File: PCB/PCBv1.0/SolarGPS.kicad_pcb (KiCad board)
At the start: 2 copper layers, 64 x 27 mm, 64 parts, among them J1 Conn_01x10_Female, J2 Solar1+, J3 GND, J4 Conn_02x05_Odd_Even, J5 Solar2+, J6 GND, J7 Screw_Terminal_01x01, U1 BQ25505, U2 MAX-M8Q, U3 MAX40200AUK, U4 STM32WB5MMGH6TR, U5 BQ25505, U6 LIS3DH, U7 TPS63802

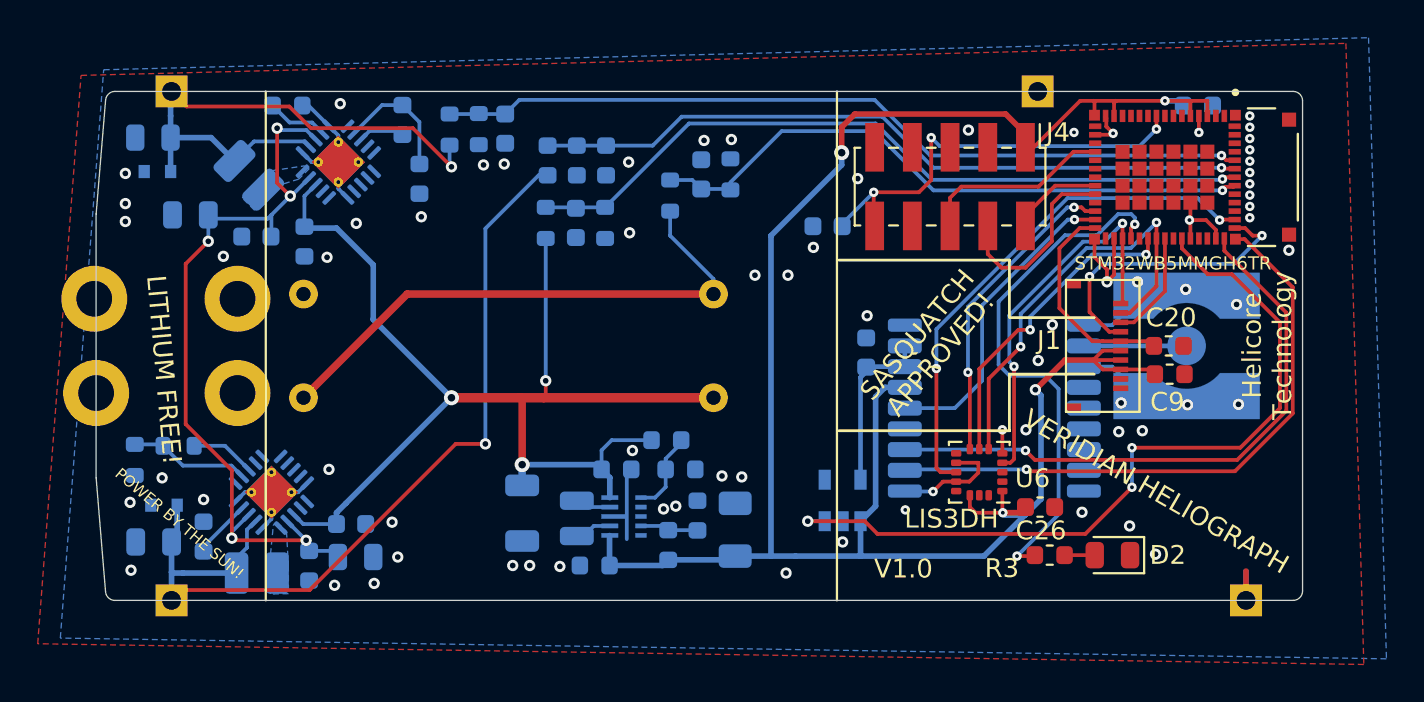
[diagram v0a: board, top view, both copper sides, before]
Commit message: Update PCB1.0 with new layout
Reverse the LCD direction for more space on the GPS signal
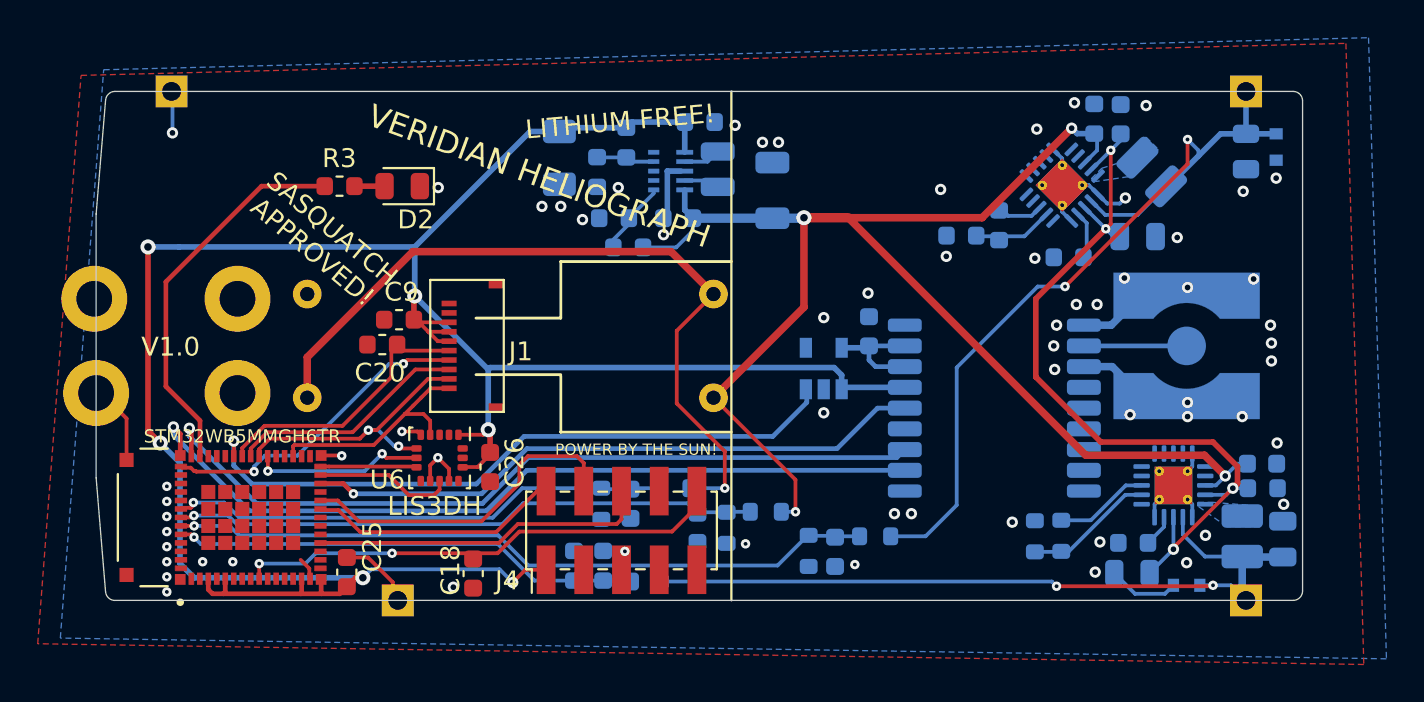
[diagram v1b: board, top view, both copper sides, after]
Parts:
- C18, C25: moved to F.Cu
- R3: value 1k -> 400
- R4: value 470k -> 412k
- U2: value MAX-M8Q -> MAX-M10Q
- moved C1 59.9 mm to (112.0, 73.8), turned to 90 degrees
- moved D3 59.4 mm to (111.6, 53.0), turned to 270 degrees
- moved C3 58.0 mm to (110.0, 53.2), turned to 270 degrees
- moved J2 57.0 mm to (110.0, 50.0)
- moved J5 57.0 mm to (110.0, 77.0)
- moved U4 54.7 mm to (55.6, 72.6), turned to 90 degrees
- moved D4 54.4 mm to (106.8, 76.2)
- moved L1 52.3 mm to (109.8, 73.6), turned to 90 degrees
- moved C25 51.5 mm to (62.3, 75.5), turned to 90 degrees
- moved C19 50.8 mm to (110.9, 71.0), turned to 180 degrees
- moved C2 50.3 mm to (104.2, 57.7), turned to 180 degrees
- moved C13 49.3 mm to (104.0, 74.0), turned to 180 degrees
- moved C11 48.4 mm to (110.8, 69.8)
- moved ROV1 47.9 mm to (98.8, 73.6), turned to 90 degrees
- moved L3 47.9 mm to (105.0, 54.3), turned to 135 degrees
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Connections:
- U4 pad 28: LIS_CS -> GPS_EXINT
- U4 pad 29: GPS_EXINT -> LIS_INT
- U4 pad 30: DISP_EN -> LIS_CS
- U4 pad 33: GND -> Net-(U4-Pad33)
- U4 pad 35: LED -> Net-(U4-Pad35)
- U4 pad 40: Net-(U4-Pad40) -> DISP_EN
- U4 pad 42: GND -> Net-(U4-Pad42)
- U4 pad 45: GND -> LED
- U4 pad 49: LIS_INT -> Net-(U4-Pad49)
- U4 pad 55: SOLAR_SENSE2 -> SOLAR_SENSE1
- U4 pad 56: SOLAR_SENSE1 -> SOLAR_SENSE2
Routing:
- net LIS_INT: track 27.7 -> 7.34 mm, vias 2 -> 0
- net VDD: track 109.2 -> 128.2 mm, vias 4 -> 6
- net GPS_EXINT: track 16.6 -> 33.1 mm
- net SOLAR1+: track 29.7 -> 44.4 mm, vias 1 -> 2
- net VBAT: track 64.7 -> 79.3 mm, vias 3 -> 4
- net SOLAR_SENSE2: track 38.2 -> 25.1 mm
- net VBATMID: track 29.6 -> 41.3 mm, vias 0 -> 1
- net LIS_CS: track 16.6 -> 5.11 mm, vias 2 -> 0
- net GPS_UART_MISO: track 32.7 -> 43.4 mm
- net GPS_UART_MOSI: track 32.1 -> 42.6 mm
- net VBAT_SENSE: track 39.7 -> 31.1 mm
- net /SWDIO: track 4.91 -> 13.4 mm
- net SPI_CLK: track 20.7 -> 12.3 mm, vias 2 -> 0
- net SPI_MOSI: track 23.0 -> 14.9 mm
- net /SWDCLK: track 10.3 -> 18.1 mm
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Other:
- board text removed: "Helicore Technology"

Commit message: Cost reduction, remove second mppt
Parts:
- removed C1, C21: 4.7uF, Capacitor_SMD:C_0805_2012Metric
- removed C10, C11, C13, C22: 10nF, Capacitor_SMD:C_0603_1608Metric
- removed L1: 22uH, Inductor_SMD:L_1008_2520Metric
- removed R7, R8: 1M, Resistor_SMD:R_0603_1608Metric
- removed ROV1: 4.32M, Resistor_SMD:R_0603_1608Metric
- removed ROV2: 8.66M, Resistor_SMD:R_0603_1608Metric
- removed U1: BQ25505, Package_DFN_QFN:QFN-20-1EP_3.5x3.5mm_P0.5mm_EP2x2mm_ThermalVias
- added D1: Schottky, Diode_SMD:D_SOD-323_HandSoldering, B.Cu at (110.0, 73.6)
- D3: value 5.1V -> Schottky; footprint Diode_SMD:D_SOD-523 -> Diode_SMD:D_SOD-323_HandSoldering
- moved C19 21.0 mm to (103.4, 51.4), turned to 270 degrees
- moved D4 20.6 mm to (111.8, 56.2), turned to 270 degrees
- moved C3 3.21 mm to (110.0, 56.4)
- moved D3 1.60 mm to (110.0, 52.9), turned to 90 degrees
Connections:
- C3 pad 1: SOLAR1+ -> SOLAR+
- D3 pad 1: SOLAR1+ -> SOLAR+
- D3 pad 2: GND -> Net-(D3-Pad2)
- D4 pad 1: SOLAR2+ -> SOLAR+
- J2 pad 1: SOLAR1+ -> Net-(D3-Pad2)
- J5 pad 1: SOLAR2+ -> Net-(D1-Pad2)
- L3 pad 1: SOLAR1+ -> SOLAR+
- R14 pad 2: SOLAR1+ -> SOLAR+
- U5 pad 2: SOLAR1+ -> SOLAR+
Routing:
- net SOLAR+: track 0.00 -> 58.2 mm, vias 0 -> 2
- net SOLAR1+: track 44.4 -> 0.00 mm, vias 2 -> 0
- net SOLAR2+: track 40.5 -> 0.00 mm, vias 2 -> 0
- net VSTOR: track 43.1 -> 9.30 mm, vias 4 -> 2
- net VBAT: track 79.3 -> 49.9 mm, vias 4 -> 3
- net SOLAR_SENSE2: track 25.1 -> 0.00 mm, vias 1 -> 0
- net VDD: track 128.2 -> 110.7 mm, vias 6 -> 7
- net GND: track 46.8 -> 37.8 mm, vias 64 -> 89
- net Net-(ROV1-Pad1): track 6.92 -> 0.00 mm
- net Net-(ROV2-Pad1): track 5.03 -> 0.00 mm
- net VBATMID: track 41.3 -> 43.7 mm
- net Net-(D1-Pad2): track 0.00 -> 1.88 mm
- net Net-(C13-Pad1): track 1.71 -> 0.00 mm
- net Net-(D3-Pad2): track 0.00 -> 1.43 mm
- removed copper zone on B.Cu, net Net-(L1-Pad2)

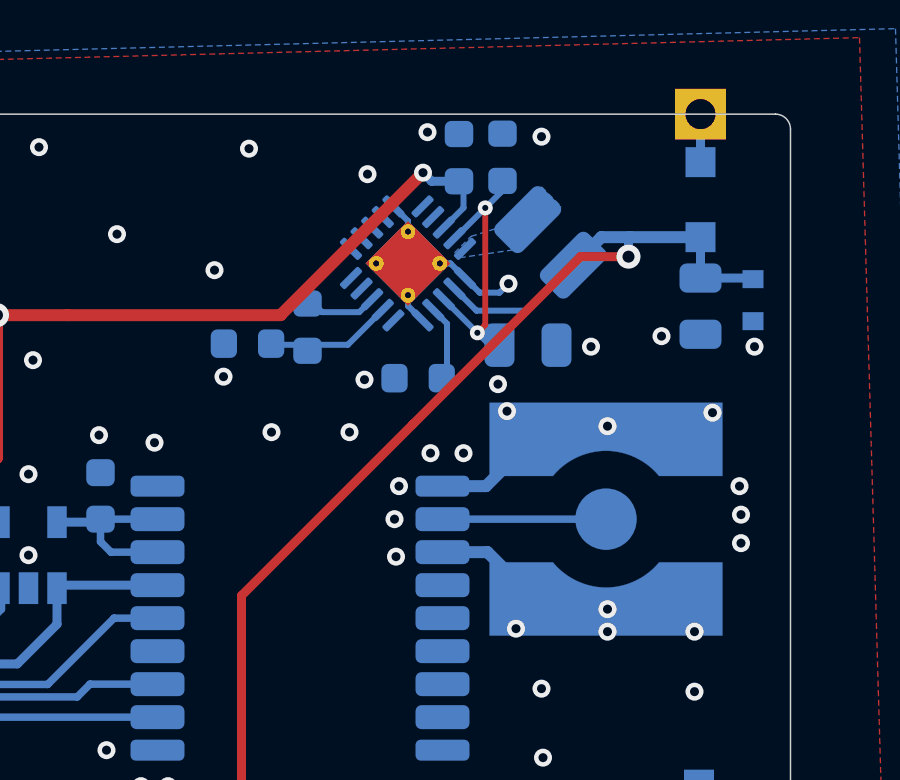
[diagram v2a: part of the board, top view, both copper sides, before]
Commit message: Update BOM, start treebuilders
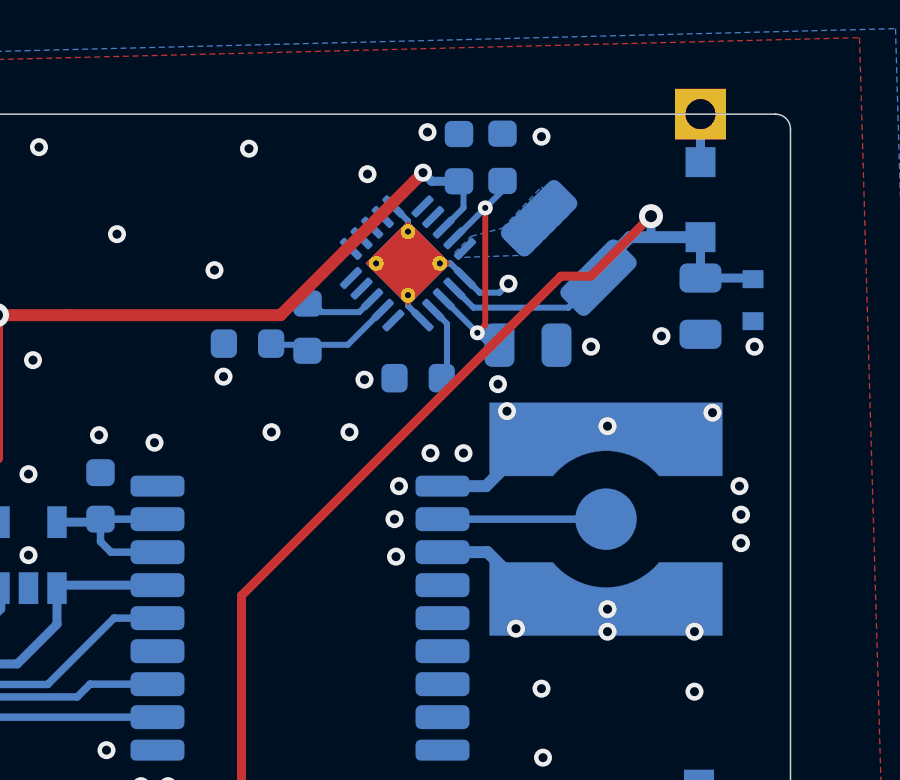
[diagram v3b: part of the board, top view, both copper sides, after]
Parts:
- L3: footprint Inductor_SMD:L_1008_2520Metric -> Inductor_SMD:L_1210_3225Metric
- moved L3 0.64 mm to (105.6, 54.5)
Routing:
- net SOLAR+: track 58.2 -> 59.1 mm

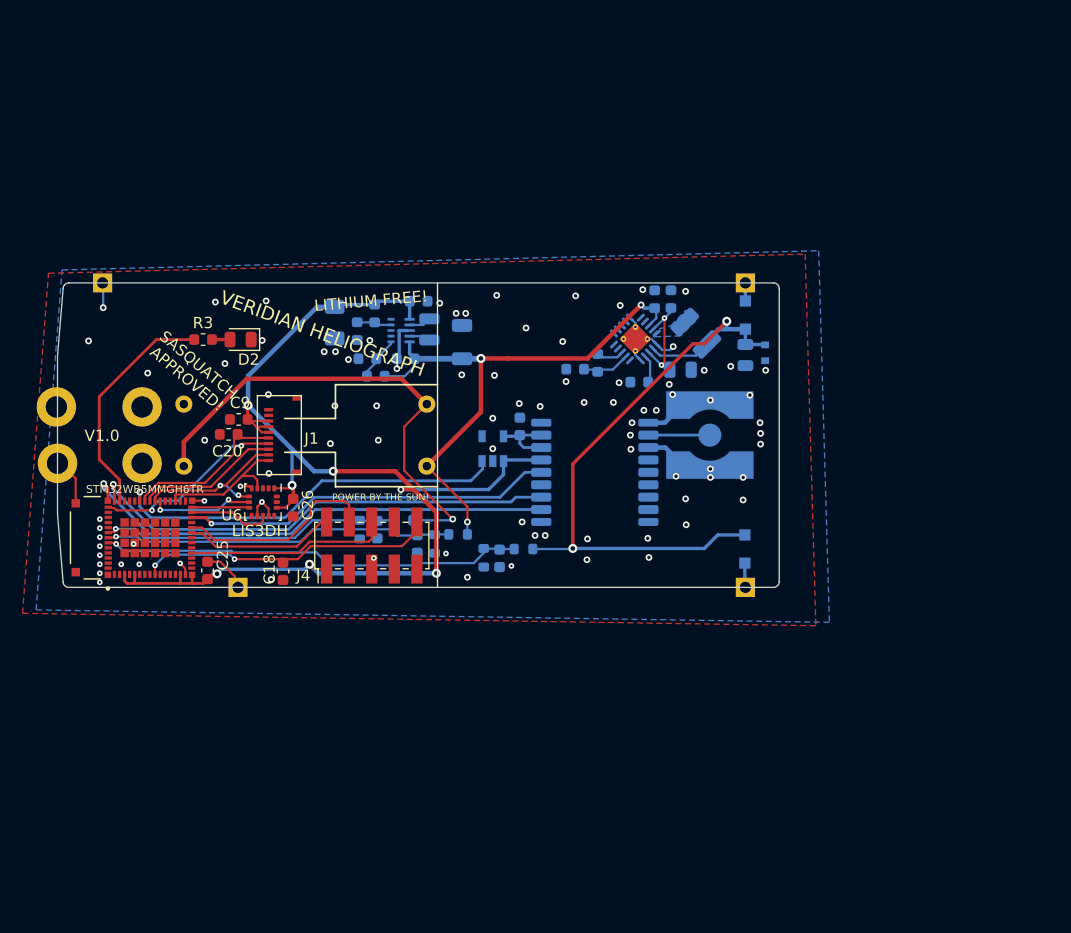
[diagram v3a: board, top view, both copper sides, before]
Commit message: Replace Antenna
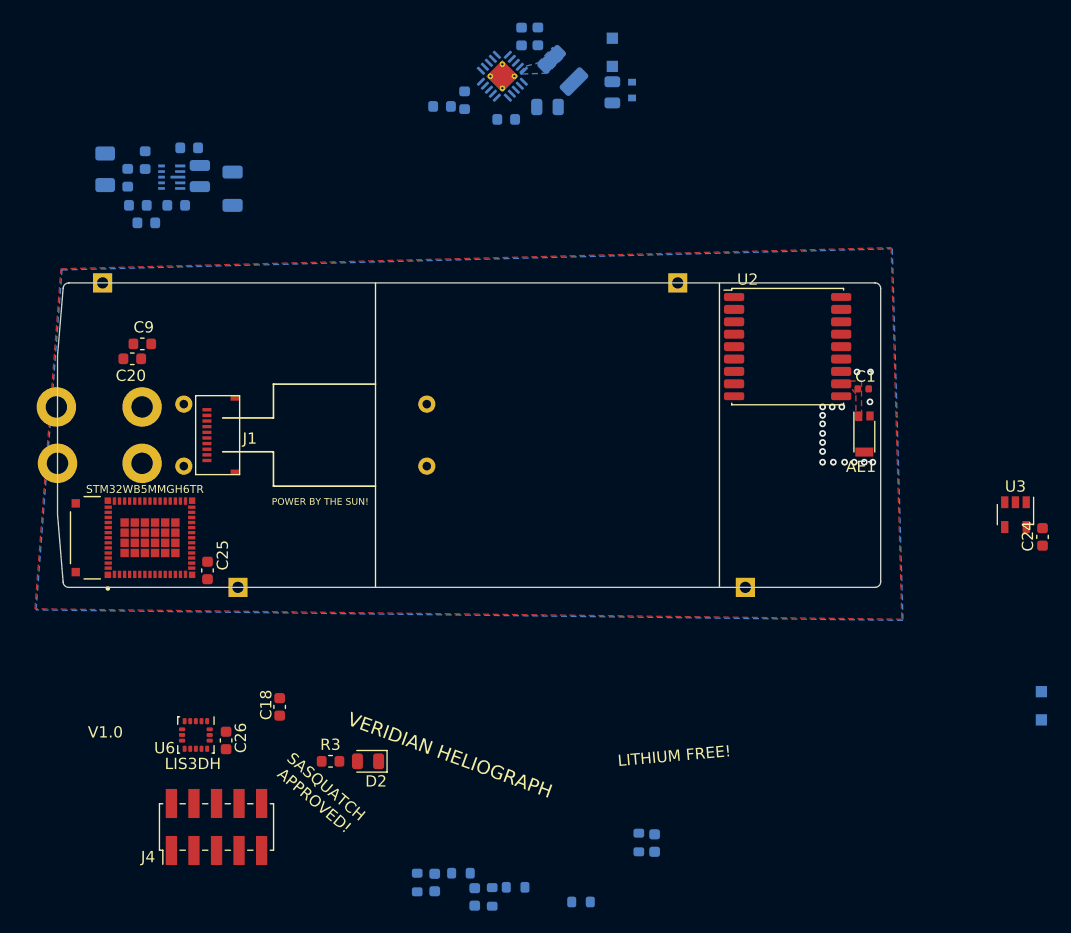
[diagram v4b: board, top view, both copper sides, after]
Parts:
- added C1: 3.3pF, Capacitor_SMD:C_0402_1005Metric, F.Cu at (120.5, 59.4)
- AE1: footprint Margo_Lib:LINX_CONSMA002-SMD -> RF_Antenna:Pulse_W3011; moved to F.Cu
- C24, U2, U3: moved to F.Cu
- R3: value 400 -> 390
- ROV3: value 4.32M -> 4.30M
- moved C24 47.4 mm to (136.3, 72.5), turned to 270 degrees
- moved U3 46.7 mm to (133.9, 70.5), turned to 270 degrees
- moved D2 39.1 mm to (76.5, 92.4)
- moved R3 39.1 mm to (73.2, 92.4)
- moved R14 31.7 mm to (95.4, 104.9)
- moved C16 31.7 mm to (82.5, 103.2)
- moved R2 31.7 mm to (84.8, 102.3)
- moved R6 31.7 mm to (80.9, 103.2)
- moved C23 31.7 mm to (86.0, 104.5)
- moved R12 31.7 mm to (89.6, 103.6)
- moved R13 31.7 mm to (87.5, 104.5)
- moved D1 29.7 mm to (136.2, 87.5)
- moved C28 28.8 mm to (102.0, 99.7)
- moved R15 28.8 mm to (100.5, 99.6)
- moved J4 28.5 mm to (63.1, 98.2)
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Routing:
- net VDD: track 110.7 -> 0.00 mm, vias 7 -> 0
- net SOLAR+: track 59.1 -> 0.00 mm, vias 2 -> 0
- net VBAT: track 49.9 -> 0.00 mm, vias 3 -> 0
- net VBATMID: track 43.7 -> 0.00 mm, vias 1 -> 0
- net GPS_UART_MISO: track 43.4 -> 0.00 mm, vias 1 -> 0
- net GPS_UART_MOSI: track 42.6 -> 0.00 mm, vias 1 -> 0
- net GND: track 37.8 -> 0.00 mm, vias 89 -> 17
- net SOLAR_SENSE1: track 37.7 -> 0.00 mm, vias 1 -> 0
- net GPSEN: track 35.5 -> 0.00 mm, vias 1 -> 0
- net GPS_EXINT: track 33.1 -> 0.00 mm, vias 1 -> 0
- net VBAT_SENSE: track 31.1 -> 0.00 mm, vias 1 -> 0
- net RESET: track 26.7 -> 0.00 mm, vias 2 -> 0
- net VBATMID_SENSE: track 26.6 -> 0.00 mm, vias 1 -> 0
- net LED: track 20.5 -> 0.00 mm
- net /SWDCLK: track 18.1 -> 0.00 mm
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- added copper zone on F.Cu, net /GPS_RF
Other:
- board size 64 x 27 mm -> 73 x 27 mm

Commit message: Redraw PCB1.0
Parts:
- added C10: 3.3pF, Capacitor_SMD:C_0402_1005Metric, F.Cu at (55.1, 68.4)
- added C11: 3.3pF, Capacitor_SMD:C_0402_1005Metric, F.Cu at (52.8, 67.7)
- added C13: 3.3pF, Capacitor_SMD:C_0402_1005Metric, F.Cu at (53.8, 67.4)
- C12, C15, C16, C19, C2, C23, C28, C3, C4, C5, C6, C7, C8, D1, D3, D4, L2, L3, R1, R12, R13, R14, R15, R2, R4, R5, R6, ROV3, ROV4, U5, U7: moved to F.Cu
- moved D1 69.4 mm to (75.1, 54.6), turned to 0 degrees
- moved R14 59.6 mm to (61.6, 55.8), turned to 90 degrees
- moved C28 57.5 mm to (63.0, 57.4)
- moved R15 55.6 mm to (64.3, 57.4)
- moved R6 44.1 mm to (111.9, 71.8), turned to 180 degrees
- moved C16 43.9 mm to (111.8, 70.5), turned to 180 degrees
- moved C23 40.7 mm to (112.0, 73.2), turned to 180 degrees
- moved R2 40.0 mm to (109.0, 70.5), turned to 180 degrees
- moved D2 38.8 mm to (53.2, 61.4), turned to 270 degrees
- moved R13 38.5 mm to (112.0, 74.8), turned to 180 degrees
- moved C15 36.7 mm to (68.3, 57.5), turned to 0 degrees
- moved R12 36.1 mm to (109.2, 73.2), turned to 180 degrees
- moved R3 34.6 mm to (53.0, 64.4), turned to 90 degrees
- moved D4 34.5 mm to (74.5, 56.2), turned to 0 degrees
- moved C19 34.3 mm to (71.5, 55.9), turned to 180 degrees
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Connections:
- net SOLAR_SENSE2 renamed Net-(U4-Pad56)
- U4 pad 42: Net-(U4-Pad42) -> GND
- U4 pad 75: GND -> Net-(U4-Pad75)
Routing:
- net VDD: track 0.00 -> 145.4 mm, vias 0 -> 2
- net VBAT: track 0.00 -> 75.1 mm, vias 0 -> 2
- net GPS_UART_MISO: track 0.00 -> 69.4 mm, vias 0 -> 2
- net GPS_UART_MOSI: track 0.00 -> 68.5 mm, vias 0 -> 2
- net VBAT_SENSE: track 0.00 -> 61.5 mm, vias 0 -> 2
- net SOLAR_SENSE1: track 0.00 -> 61.2 mm, vias 0 -> 4
- net VBATMID_SENSE: track 0.00 -> 60.9 mm, vias 0 -> 2
- net GPSEN: track 0.00 -> 59.1 mm, vias 0 -> 2
- net GPS_EXINT: track 0.00 -> 56.8 mm, vias 0 -> 2
- net VBATMID: track 0.00 -> 54.3 mm
- net Net-(D1-Pad2): track 0.00 -> 52.1 mm, vias 0 -> 2
- net Net-(D3-Pad2): track 0.00 -> 34.5 mm
- net GND: track 0.00 -> 27.1 mm, vias 17 -> 108
- net SOLAR+: track 0.00 -> 24.6 mm, vias 0 -> 2
- net RESET: track 0.00 -> 23.5 mm, vias 0 -> 2
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- added copper zone on F.Cu, net Net-(L3-Pad2)
- removed copper zone on B.Cu, net Net-(L3-Pad2)
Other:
- outline, holes or cut-outs redrawn
- rule trace_min: 0.16 -> 0.2
- board text added: "APPLY DIRECTLY TO EYEBALLS"
- board text added: "DONT LOOK HERE"
- board text removed: "POWER BY THE SUN!"
